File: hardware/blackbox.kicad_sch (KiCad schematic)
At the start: 3 parts

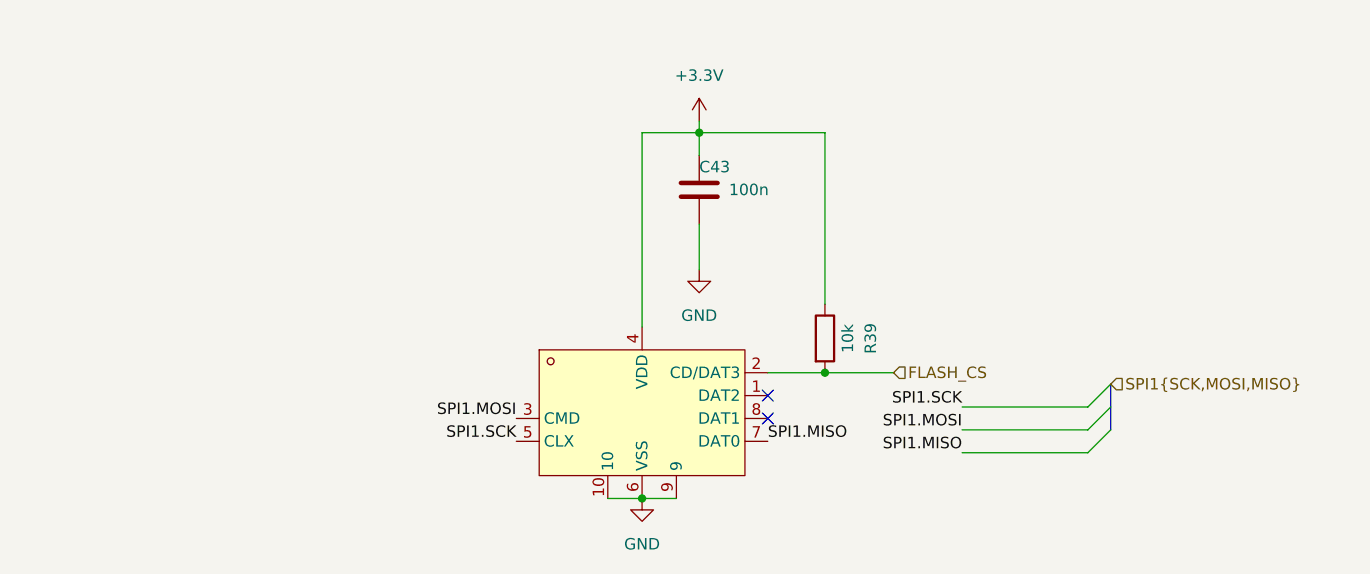
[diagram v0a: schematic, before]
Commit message: Rev 2 (RP2354A): finalize design, update docs, clean repo (#5)
* docs(readme): add analog OSD BOM to Rev 2 change list

Document OSD debugging findings and component changes as a new
Analog OSD section in the Rev 2 Change List:
- HW-12: U19 op-amp TLV9061IDPWR -> COS8051SOT (175MHz video-grade RRIO)
- HW-13: output front-end add AC-couple + DC-restore, power U19 from +5V
- HW-14: U20 comparator TLV3201AIDBVR -> TLV7031DPWR (push-pull, X2SON, ~75% smaller)
- HW-15: add OSD_EN select pull-down (datasheet-required, defaults to pass-through)
- U18 / D9 verified correct, no change; OSD GPIO mapping noted (PA4/5/6)

Also fix HW-11 beeper GPIO: GPIO6 -> GPIO7 (GPIO6 is OSD_SYNC per netlist).

Co-Authored-By: Claude Opus 4.8 (1M context) <noreply@anthropic.com>

* many tiny improvements

- I/O correctness
- SPI0/SPI1/I2C0 bus corrections
- decoupling of DVDD
- ADC_AVDD as per RPi documents
- removal of SBUS
- connect ESC serial
- remove RUN RC-circuit as per RPi documentation
- some more cleanup for readability
- gyro CLKIN decision
- I2C 4.7k pullup

* RP2354A

* piu1

* switch spi

* Update OpenFC.kicad_pcb

* routex2

* some minor tweaks

- remove some unnecessary resistors
- slightly higher 10V rail to account for voltage drop
- some cleanup
- simpler PG 1.8V circuit

* Update imu.kicad_sch

* LED resistors

Also reduced the amount of different resistors for cheaper assembly

* Delete leds.kicad_sch

* remove some unneeded decoupling caps from RP2350

* update MOSFET part numbers

* OSD

* ROUTE

* clean libs

* details

* led names

* Clean routing

* docs: rewrite README + CLAUDE.md for finalized Rev 2 (RP2354A)

Rev 2 is a substantial redesign that the docs no longer matched. Updated
both to the actual schematic, verified from the current netlist:

- MCU: RP2354B (QFN-80, GPIO0-47) -> RP2354A (QFN-60, GPIO0-29). Full GPIO
  map re-derived from the netlist + QFN-60 pinout; all 30 GPIO documented.
- IMU moved to SPI1, microSD to SPI0; ref designators re-annotated
  (op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
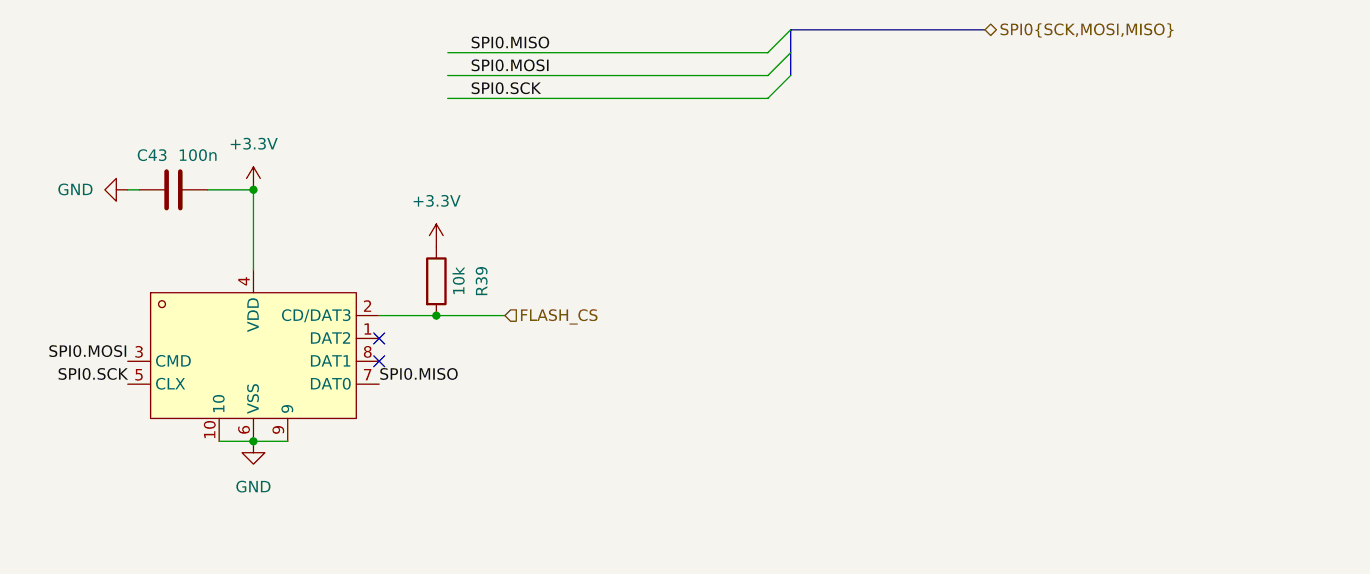
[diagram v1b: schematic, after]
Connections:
- net SPI1.MISO renamed SPI0.MISO
- net SPI1.MOSI renamed SPI0.MOSI
- net SPI1.SCK renamed SPI0.SCK
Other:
- moved on the sheet: C43, R39
